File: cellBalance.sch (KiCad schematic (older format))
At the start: 7 parts, among them Q5 Q_PMOS_GSD

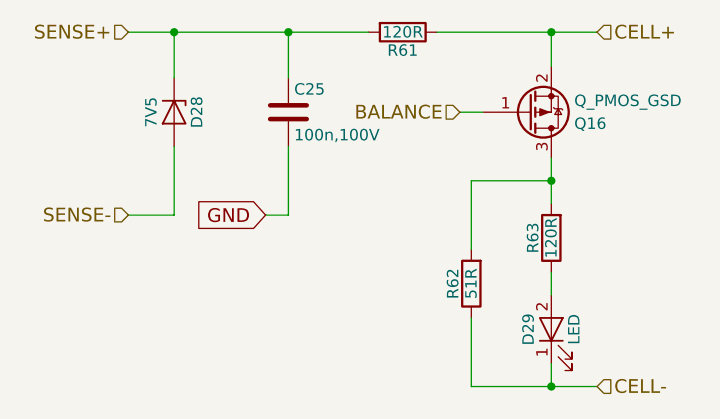
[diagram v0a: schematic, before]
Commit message: HW 0.2 finalized schematic and pcb files, BOM needs to be checked
Lots of major and little problems fixed found in the 0.1

Major changes:
-LTC6803-3 footprint changed to it's correct one
-Boost converter layout and capacitor optimization
-MCU switched from STM32F070CBT6 to ultra low power STM32L433CCT6 to improve sleep state power consumption
-Button/LED + Comms connectors switched from THT JST-XH to SMD JST-PH
-CAN-bus support added
-Changed power regulator setup for "always on"

Minor changes:
-Changed cell balance resistor sizes from 0603 to 0402 in order to get a bit more breathing room during soldering
-External oscillator removed from MCU, because new one has everything available internally
-Comms connector has USART or CAN available via solder bridges
-Sense resistors switched to higher resistance ones to lower deep sleep standby current
-etc.
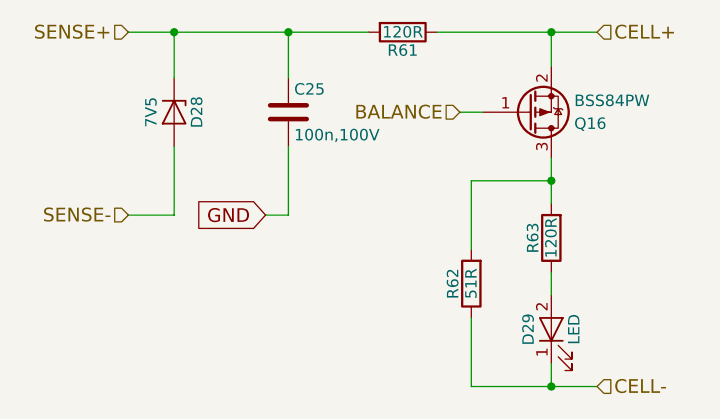
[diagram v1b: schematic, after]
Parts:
- C14: MFG CL10B104KC8NNNC -> ANY; TempCo. (none) -> X7R
- Q5: value Q_PMOS_GSD -> BSS84PW
- R28, R30: footprint Resistors_SMD:R_0603 -> Resistors_SMD:R_0402; MFG RC0603FR-07120RL -> ANY; Tol. (none) -> 1%
- R29: MFG RC1206FR-0751RL -> ANY; Power (none) -> 0.5W; Tol. (none) -> 5%
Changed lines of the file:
@@
 LIBS:valves
 LIBS:Custom_comp_lib
-LIBS:FlexiBMS_01-cache
+LIBS:FlexiBMS-cache
 EELAYER 25 0
 EELAYER END
@@
 Title "FlexiBMS"
 Date "2018-02-22"
-Rev "0.1"
+Rev "0.2"
 Comp "SiMoS MCmuffin / Simo Sihvonen"
 Comment1 ""
@@
 F 0 "R61" V 6430 2600 50  0000 C CNN
 F 1 "120R" V 6350 2600 50  0000 C CNN
-F 2 "Resistors_SMD:R_0603" V 6280 2600 50  0001 C CNN
+F 2 "Resistors_SMD:R_0402" V 6280 2600 50  0001 C CNN
 F 3 "" H 6350 2600 50  0001 C CNN
-F 4 "RC0603FR-07120RL" V 6350 2600 60  0001 C CNN "MFG"
+F 4 "ANY" V 6350 2600 60  0001 C CNN "MFG"
+F 5 "1%" V 6350 2600 60  0001 C CNN "Tol."
 	1    6350 2600
 	0    1    1    0
@@
 F 0 "R63" V 7080 3500 50  0000 C CNN
 F 1 "120R" V 7000 3500 50  0000 C CNN
-F 2 "Resistors_SMD:R_0603" V 6930 3500 50  0001 C CNN
+F 2 "Resistors_SMD:R_0402" V 6930 3500 50  0001 C CNN
 F 3 "" H 7000 3500 50  0001 C CNN
-F 4 "RC0603FR-07120RL" V 7000 3500 60  0001 C CNN "MFG"
+F 4 "ANY" V 7000 3500 60  0001 C CNN "MFG"
+F 5 "1%" V 7000 3500 60  0001 C CNN "Tol."
 	1    7000 3500
 	-1   0    0    1
@@
 F 2 "Resistors_SMD:R_0805" V 6580 3700 50  0001 C CNN
 F 3 "" H 6650 3700 50  0001 C CNN
-F 4 "RC1206FR-0751RL" V 6650 3700 60  0001 C CNN "MFG"
+F 4 "ANY" V 6650 3700 60  0001 C CNN "MFG"
+F 5 "5%" V 6650 3700 60  0001 C CNN "Tol."
+F 6 "0.5W" V 6650 3700 60  0001 C CNN "Power"
 	1    6650 3700
 	-1   0    0    1
@@
 F 2 "Capacitors_SMD:C_0603" H 5888 2800 50  0001 C CNN
 F 3 "" H 5850 2950 50  0001 C CNN
-F 4 "CL10B104KC8NNNC" H 5850 2950 60  0001 C CNN "MFG"
+F 4 "ANY" H 5850 2950 60  0001 C CNN "MFG"
+F 5 "X7R" H 5850 2950 60  0001 C CNN "TempCo."
 	1    5850 2950
 	1    0    0    -1
@@
 AR Path="/5A82A74A/5A82F760/5A82AE4B" Ref="Q14"  Part="1"
 F 0 "Q16" H 7100 3000 50  0000 L CNN
-F 1 "Q_PMOS_GSD" H 7100 2900 50  0000 L CNN
+F 1 "BSS84PW" H 7100 2900 50  0000 L CNN
 F 2 "TO_SOT_Packages_SMD:SOT-323_SC-70" H 7100 3050 50  0001 C CNN
 F 3 "" H 6900 2950 50  0001 C CNN
